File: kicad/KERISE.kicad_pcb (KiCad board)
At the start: 2 copper layers, 41 x 38.7 mm, 97 parts, among them J1 Motor_L, J10 ENC_Host, J11 ENC_Slave, J12 Host, J13 Slave, J14 Host, J15 Slave, J2 Motor_R, J3 Host, J4 Slave, J5 Host, J6 Slave, J7 COM, J8 ENC_Host, J9 ENC_Slave, P1 ToF_Host, P2 ToF_Slave, Q1 MTM231232LBF, Q10 MTM231232LBF, Q11 DMN3065LW-7, Q12 SFH3015FA, Q13 DMN3065LW-7, Q2 DMN3065LW-7, Q3 SFH3015FA, Q4 MTM231232LBF, Q5 DMN3065LW-7, Q6 SFH3015FA, Q7 MTM231232LBF, Q8 DMN3065LW-7, Q9 SFH3015FA, SW1 RESET, SW2 UPLOAD, U1 ESP32-PICO-D4, U2 DRV8835, U3 LXDC2UR30, U4 MA730, U5 MA730, U6 ICM-20602, U7 PCA9632, U8 VL6180X

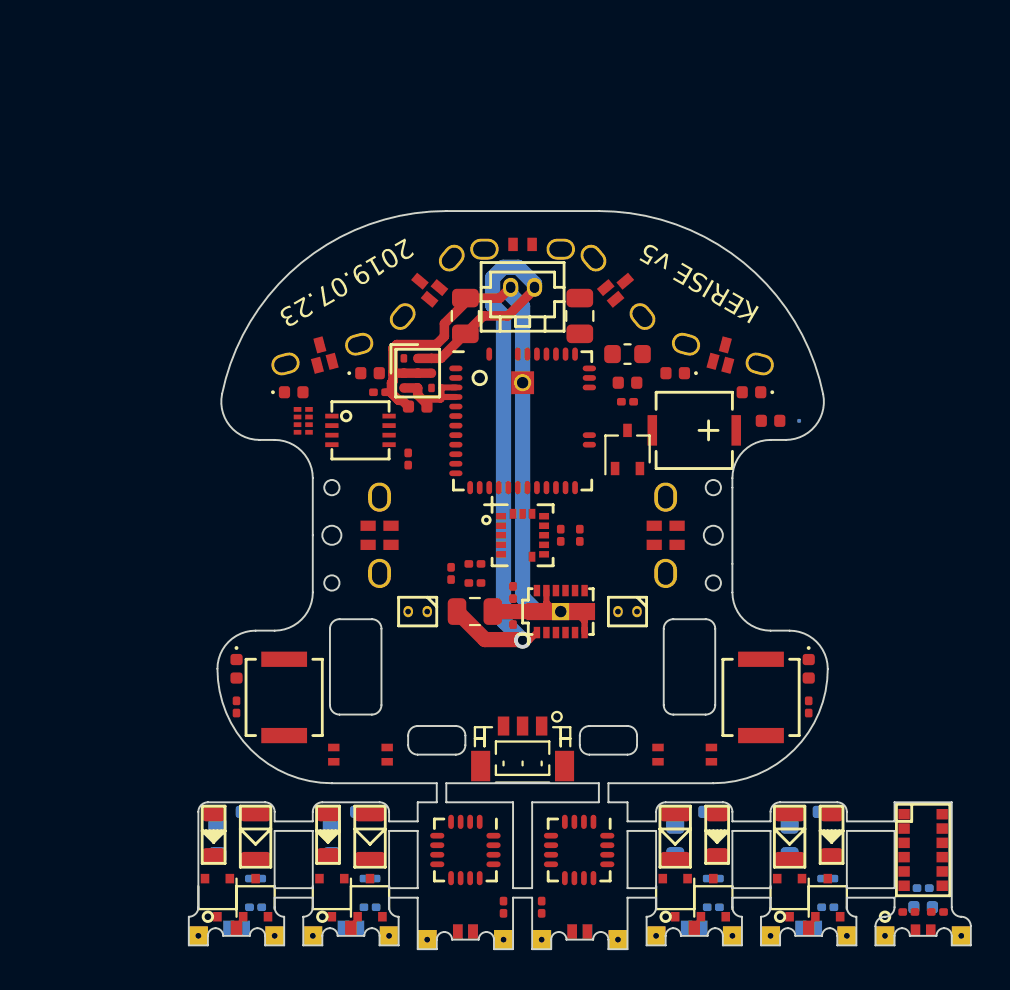
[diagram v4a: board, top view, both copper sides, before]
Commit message: fix pcb margin
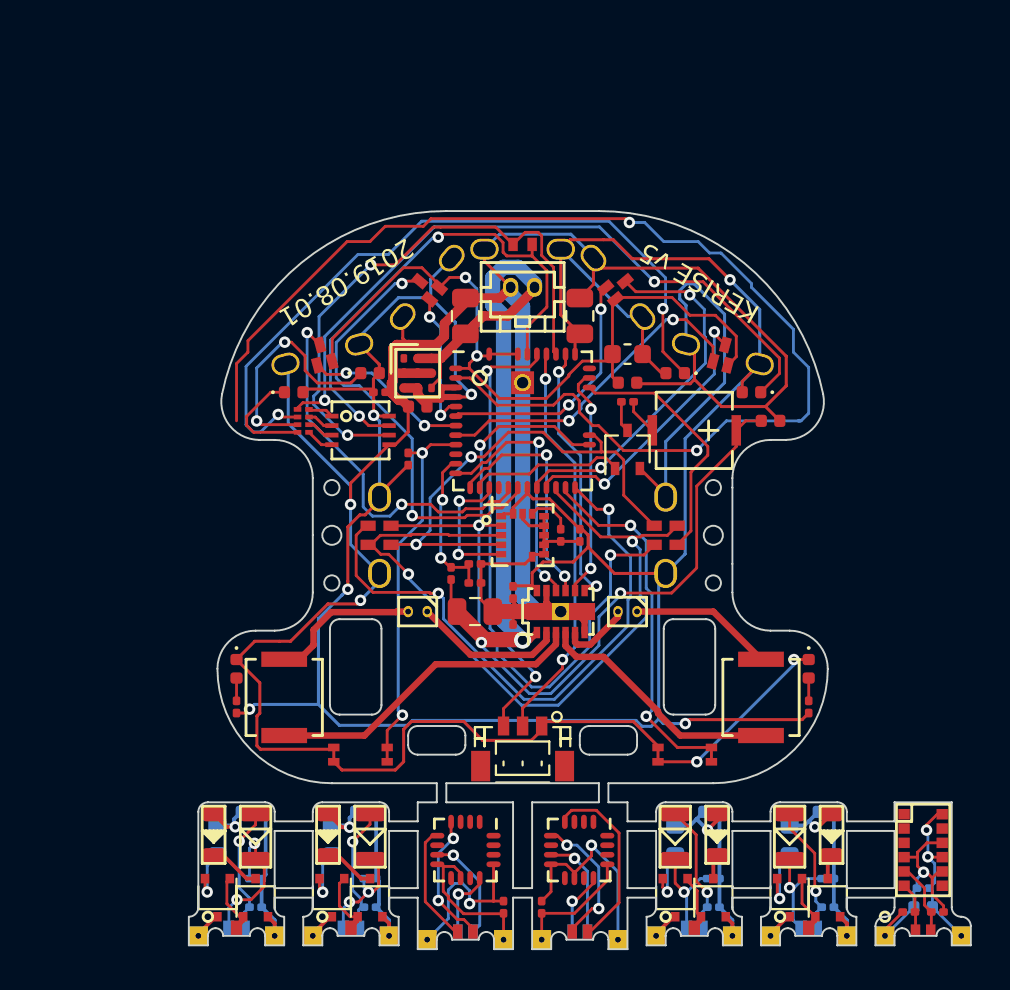
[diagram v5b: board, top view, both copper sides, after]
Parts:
- added G***: LOGO, mouse:KERI_9mm, B.Cu at (148.5, 111.0)
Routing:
- net +3V3: track 7.03 -> 151.0 mm, vias 0 -> 6
- net GND: track 40.0 -> 182.0 mm, vias 0 -> 4
- net /ANTENA: track 0.00 -> 64.7 mm, vias 0 -> 2
- net VDDA: track 0.00 -> 41.0 mm, vias 0 -> 2
- net SPI-MOSI: track 0.00 -> 39.9 mm, vias 0 -> 2
- net Net-(D8-Pad1): track 0.00 -> 38.3 mm, vias 0 -> 2
- net SPI-SCLK: track 0.00 -> 37.9 mm, vias 0 -> 3
- net Net-(D7-Pad1): track 0.00 -> 36.3 mm, vias 0 -> 2
- net SPI-CS-ENC_L: track 0.00 -> 31.0 mm, vias 0 -> 2
- net +BATT: track 35.3 -> 65.7 mm, vias 1 -> 3
- net I2C-SCL: track 0.00 -> 30.2 mm, vias 0 -> 2
- net I2C-SDA: track 0.00 -> 26.5 mm, vias 0 -> 2
- net SPI-MISO: track 0.00 -> 26.1 mm, vias 0 -> 2
- net UART-TX: track 0.00 -> 23.5 mm, vias 0 -> 2
- net PR-LED-SL: track 0.00 -> 23.3 mm, vias 0 -> 2
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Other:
- board text added: "2019.08.01"
- board text removed: "2019.07.23"

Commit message: 回路を修正，未配線
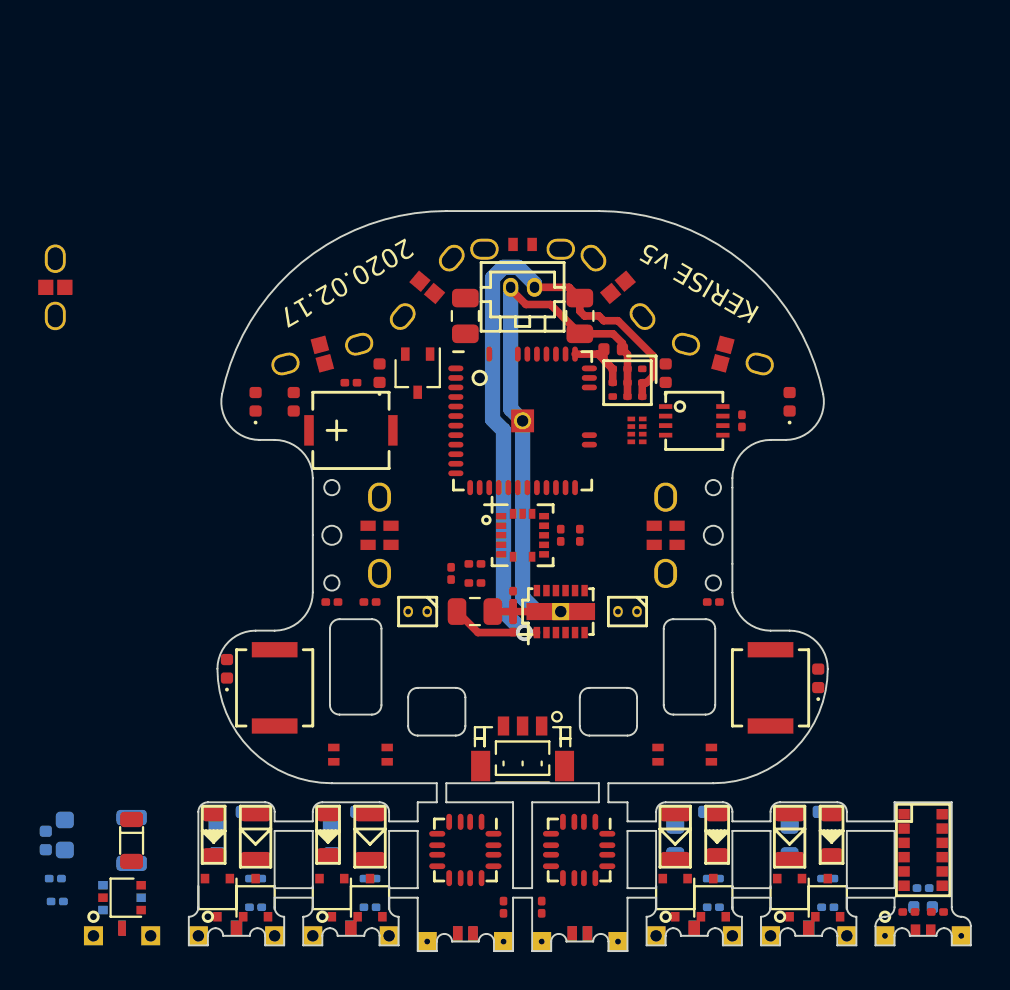
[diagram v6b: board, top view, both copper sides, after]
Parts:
- removed the C11 at (134.2, 127.5)
- removed the C12 at (134.5, 131.0)
- removed the C3 at (148.0, 118.0)
- removed the C8 at (154.0, 105.0)
- removed G***: LOGO, mouse:KERI_9mm
- removed the J3 at (143.5, 100.0)
- removed the J6 at (133.5, 134.0)
- removed L3: 100u, Inductor_SMD:L_0603_1608Metric
- added C10: 2.2u, Capacitor_SMD:C_0402_1005Metric, B.Cu at (123.5, 129.0)
- added C10: 2.2u, Capacitor_SMD:C_0402_1005Metric, B.Cu at (134.2, 127.5)
- added C11: 0.1u, Capacitor_SMD:C_0201_0603Metric, B.Cu at (124.0, 131.0)
- added C11: 0.1u, Capacitor_SMD:C_0201_0603Metric, B.Cu at (134.5, 131.0)
- added C5: 0.1u, Capacitor_SMD:C_0201_0603Metric, F.Cu at (146.0, 114.5)
- added D4: SFH4045N_L, mouse:SFH4045N_L, F.Cu at (128.0, 129.0)
- added J3: Host, mouse:IR_HOST_V_04, F.Cu at (124.0, 100.0)
- added J3: Host, mouse:IR_HOST_04, F.Cu at (143.5, 100.0)
- added J6: Slave, mouse:IR_SLAVE_04, F.Cu at (127.5, 134.0)
- added J6: Slave, mouse:IR_SLAVE_04, F.Cu at (133.5, 134.0)
- added Q4: MTM231232LBF, mouse:SOT-323_SC-70, B.Cu at (127.5, 132.0)
- added Q5: DMN3065LW-7, mouse:SOT-323_SC-70, F.Cu at (127.5, 132.0)
- added Q6: SFH3015FA_L, mouse:SFH3015FA_L, B.Cu at (128.0, 129.0)
- added R8: 100, Resistor_SMD:R_0603_1608Metric, B.Cu at (124.5, 128.7)
- added R9: 10k, Resistor_SMD:R_0201_0603Metric, B.Cu at (124.1, 132.2)
- AE1: moved to F.Cu
- C14: renamed from C15; value 1u -> 2.2u
- C16: renamed from C17; value 1u -> 2.2u
- C8: renamed from C9; value 1u -> 2.2u
- J12, J14, J5: footprint mouse:STAND_HOST_05 -> mouse:IR_HOST_04
- J13, J15, J4: footprint mouse:STAND_SLAVE_05 -> mouse:IR_SLAVE_04
- moved C21 25.0 mm to (136.5, 106.0), turned to 90 degrees
- moved C20 19.1 mm to (160.0, 107.0), turned to 270 degrees
- moved AE1 18.1 mm to (145.0, 104.8)
- moved LS1 18.0 mm to (139.5, 107.5), turned to 0 degrees
- moved RN1 17.5 mm to (154.5, 107.5)
- moved U7 17.5 mm to (157.5, 107.0)
- moved R14 14.5 mm to (139.5, 105.0), turned to 0 degrees
- moved Q13 11.7 mm to (143.0, 104.5), turned to 270 degrees
- moved U3 11.0 mm to (154.0, 105.0), turned to 0 degrees
- moved C1 10.7 mm to (153.2, 103.2), turned to 180 degrees
- moved R1 7.76 mm to (140.5, 116.5), turned to 180 degrees
- moved R4 7.43 mm to (138.5, 116.5), turned to 180 degrees
- moved R5 7.43 mm to (158.5, 116.5), turned to 0 degrees
- moved C6 6.00 mm to (151.5, 101.5), turned to 270 degrees
- moved C7 6.00 mm to (145.5, 101.5)
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- renumbered C13 to C12, C14 to C13, C16 to C15, C18 to C17, C19 to C18, C20 to C19, C21 to C20, C22 to C21, C23 to C22, C24 to C23, C4 to C3, C5 to C4, C10 to C9
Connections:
- C15 pad 1: /IR_RCV_FL/s_AVDD -> /IR_RCV_FL/s_3.3V
- C17 pad 1: /IR_RCV_FR/s_AVDD -> /IR_RCV_FR/s_3.3V
- C3 pad 1: +3V3 -> +BATT
- C4 pad 1: BAT-VOL -> +3V3
- C9 pad 1: /IR_RCV_SL/s_AVDD -> /IR_RCV_SL/s_3.3V
- J12 pad 2: VDDA -> PR-LED-FL
- J12 pad 3: PR-LED-FL -> PR-RCV-FL
- J12 pad 4: PR-RCV-FL -> GND
- J13 pad 2: /IR_RCV_FL/s_AVDD -> /IR_RCV_FL/s_IR_LED
- J13 pad 3: /IR_RCV_FL/s_IR_LED -> /IR_RCV_FL/s_IR_RCV
- J13 pad 4: /IR_RCV_FL/s_IR_RCV -> /IR_RCV_FL/s_GND
- J14 pad 2: VDDA -> PR-LED-FR
- J14 pad 3: PR-LED-FR -> PR-RCV-FR
- J14 pad 4: PR-RCV-FR -> GND
- J15 pad 2: /IR_RCV_FR/s_AVDD -> /IR_RCV_FR/s_IR_LED
- J15 pad 3: /IR_RCV_FR/s_IR_LED -> /IR_RCV_FR/s_IR_RCV
- J15 pad 4: /IR_RCV_FR/s_IR_RCV -> /IR_RCV_FR/s_GND
- J4 pad 2: /IR_RCV_SL/s_AVDD -> /IR_RCV_SL/s_IR_LED
- J4 pad 3: /IR_RCV_SL/s_IR_LED -> /IR_RCV_SL/s_IR_RCV
- J4 pad 4: /IR_RCV_SL/s_IR_RCV -> /IR_RCV_SL/s_GND
- J5 pad 2: VDDA -> PR-LED-SR
- J5 pad 3: PR-LED-SR -> PR-RCV-SR
- J5 pad 4: PR-RCV-SR -> GND
- Q1 pad 2: Net-(Q1-Pad2) -> /IR_RCV_SL/s_3.3V
- Q1 pad 3: /IR_RCV_SL/s_3.3V -> Net-(Q1-Pad3)
- Q10 pad 2: Net-(Q10-Pad2) -> /IR_RCV_FR/s_3.3V
- Q10 pad 3: /IR_RCV_FR/s_3.3V -> Net-(Q10-Pad3)
- Q12 pad 1: /IR_RCV_FR/s_AVDD -> /IR_RCV_FR/s_3.3V
- Q3 pad 1: /IR_RCV_SL/s_AVDD -> /IR_RCV_SL/s_3.3V
- Q4 pad 2: Net-(Q4-Pad2) -> /IR_RCV_SR/s_3.3V
- Q4 pad 3: /IR_RCV_SR/s_3.3V -> Net-(Q4-Pad3)
- Q6 pad 1: /IR_RCV_SR/s_AVDD -> /IR_RCV_SR/s_3.3V
- Q7 pad 2: Net-(Q7-Pad2) -> /IR_RCV_FL/s_3.3V
- Q7 pad 3: /IR_RCV_FL/s_3.3V -> Net-(Q7-Pad3)
- Q9 pad 1: /IR_RCV_FL/s_AVDD -> /IR_RCV_FL/s_3.3V
- R10 pad 1: Net-(Q7-Pad2) -> Net-(Q7-Pad3)
- R12 pad 1: Net-(Q10-Pad2) -> Net-(Q10-Pad3)
- R6 pad 1: Net-(Q1-Pad2) -> Net-(Q1-Pad3)
- R8 pad 1: Net-(Q4-Pad2) -> Net-(Q4-Pad3)
- U1 pad 1: VDDA -> +3V3
- U1 pad 43: VDDA -> +3V3
- U1 pad 46: VDDA -> +3V3
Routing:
- net GND: track 182.0 -> 33.3 mm, vias 4 -> 0
- net +3V3: track 151.0 -> 4.24 mm, vias 6 -> 0
- net /ANTENA: track 64.7 -> 0.00 mm, vias 2 -> 0
- net VDDA: track 41.0 -> 0.00 mm, vias 2 -> 0
- net SPI-MOSI: track 39.9 -> 0.00 mm, vias 2 -> 0
- net Net-(D8-Pad1): track 38.3 -> 0.00 mm, vias 2 -> 0
- net SPI-SCLK: track 37.9 -> 0.00 mm, vias 3 -> 0
- net Net-(D7-Pad1): track 36.3 -> 0.00 mm, vias 2 -> 0
- net SPI-CS-ENC_L: track 31.0 -> 0.00 mm, vias 2 -> 0
- net I2C-SCL: track 30.2 -> 0.00 mm, vias 2 -> 0
- net +BATT: track 65.7 -> 37.5 mm, vias 3 -> 1
- net I2C-SDA: track 26.5 -> 0.00 mm, vias 2 -> 0
- net SPI-MISO: track 26.1 -> 0.00 mm, vias 2 -> 0
- net UART-TX: track 23.5 -> 0.00 mm, vias 2 -> 0
- net PR-LED-SL: track 23.3 -> 0.00 mm, vias 2 -> 0
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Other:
- board size 41 x 38.7 mm -> 41 x 38.8 mm
- board text added: "2020.02.17"
- board text removed: "2019.08.01"

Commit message: 予備配線完了
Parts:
- removed AE1: Antenna, mouse:HIDDEN_PAD
- removed the C10 at (123.5, 129.0)
- removed the C10 at (134.2, 127.5)
- removed the C11 at (124.0, 131.0)
- removed the C11 at (134.5, 131.0)
- removed the D10 at (134.5, 106.0)
- removed the D4 at (128.0, 129.0)
- removed the D4 at (132.3, 128.7)
- removed the D9 at (141.0, 104.5)
- removed the J14 at (159.0, 103.5)
- removed the J15 at (157.5, 134.0)
- removed the J3 at (124.0, 100.0)
- removed the J3 at (143.5, 100.0)
- removed the J5 at (153.5, 100.0)
- removed the J6 at (127.5, 134.0)
- removed the J6 at (133.5, 134.0)
- removed Q10: MTM231232LBF, mouse:SOT-323_SC-70
- removed Q11: DMN3065LW-7, mouse:SOT-323_SC-70
- removed Q12: SFH3015FA, mouse:SFH3015FA
- removed Q13: DMN3065LW-7, Package_TO_SOT_SMD:SOT-323_SC-70
- removed the Q4 at (127.5, 132.0)
- removed the Q4 at (132.5, 132.0)
- removed the Q5 at (127.5, 132.0)
- removed the Q5 at (134.5, 132.0)
- removed the Q6 at (128.0, 129.0)
- removed the Q6 at (134.5, 128.8)
- removed the R13 at (158.5, 132.5)
- removed the R14 at (139.5, 105.0)
- removed the R8 at (124.5, 128.7)
- removed the R8 at (132.5, 129.0)
- removed the R9 at (124.1, 132.2)
- removed the R9 at (134.5, 132.5)
- removed the U6 at (148.5, 113.0)
- added C10: 2.2u, Capacitor_SMD:C_0402_1005Metric, F.Cu at (164.5, 132.0)
- added C11: 0.1u, Capacitor_SMD:C_0201_0603Metric, B.Cu at (165.0, 128.5)
- added D4: LED, LED_SMD:LED_0402_1005Metric, F.Cu at (139.5, 99.6)
- added D7: SFH4045N, mouse:SFH4045N_L, B.Cu at (133.8, 129.2)
- added D8: SFH4045N, mouse:SFH4045N_L, B.Cu at (139.8, 129.2)
- added J1: Host, mouse:IR_HOST_V_04, F.Cu at (159.5, 102.0)
- added J10: Host, mouse:IR_HOST_V_04, F.Cu at (154.5, 99.0)
- added J11: Slave, mouse:IR_SLAVE_V_04, F.Cu at (133.5, 134.0)
- added J2: Slave, mouse:IR_SLAVE_V_04, F.Cu at (157.5, 134.0)
- added J3: Host, mouse:IR_HOST_V_04, F.Cu at (137.5, 102.0)
- added Q4: DMN3065LW-7, mouse:SOT-323_SC-70, B.Cu at (163.5, 132.0)
- added Q5: SFH3015FA, mouse:SFH3015FA_L, B.Cu at (163.5, 129.2)
- added Q6: DMN3065LW-7, mouse:SOT-323_SC-70, F.Cu at (133.5, 132.0)
- added R11: 100, Resistor_SMD:R_0603_1608Metric, B.Cu at (138.1, 132.0)
- added R15: 1k, Resistor_SMD:R_0201_0603Metric, F.Cu at (141.0, 116.5)
- added R5: 100, Resistor_SMD:R_0603_1608Metric, F.Cu at (156.7, 132.0)
- added R9: 100, Resistor_SMD:R_0603_1608Metric, B.Cu at (132.2, 132.0)
- added U4: ICM-20602, mouse:ICM-20602, F.Cu at (148.5, 113.0)
- C15, C17, C8: moved to F.Cu
- D3: value SFH4045N -> LED; footprint mouse:SFH4045N -> LED_SMD:LED_0402_1005Metric
- D5, D6: footprint mouse:SFH4045N -> mouse:SFH4045N_L
- J12: footprint mouse:IR_HOST_04 -> mouse:IR_HOST_V_04
- J13, J4: footprint mouse:IR_SLAVE_04 -> mouse:IR_SLAVE_V_04
- Q1: value MTM231232LBF -> DMN3065LW-7; footprint mouse:SOT-323_SC-70 -> Package_TO_SOT_SMD:SOT-323_SC-70
- Q2: moved to B.Cu
- Q3: footprint mouse:SFH3015FA -> mouse:SFH3015FA_L; moved to B.Cu
- Q7: value MTM231232LBF -> SFH3015FA; footprint mouse:SOT-323_SC-70 -> mouse:SFH3015FA_L
- Q9: footprint mouse:SFH3015FA -> mouse:SFH3015FA_L
- R10, R12, R6: value 100 -> 10k; footprint Resistor_SMD:R_0603_1608Metric -> Resistor_SMD:R_0201_0603Metric
- R4: value 1k -> 10
- R7: value 10k -> 100; footprint Resistor_SMD:R_0201_0603Metric -> Resistor_SMD:R_0603_1608Metric; moved to F.Cu
- moved D3 31.4 mm to (145.0, 98.0)
- moved C15 29.5 mm to (135.0, 130.2), turned to 270 degrees
- moved C14 29.5 mm to (135.0, 128.5), turned to 270 degrees
- moved Q7 29.1 mm to (133.5, 129.2), turned to 90 degrees
- moved R10 28.0 mm to (134.8, 132.5), turned to 0 degrees
- moved Q1 27.9 mm to (143.0, 104.5)
- moved Q8 25.0 mm to (139.5, 132.0), turned to 180 degrees
- moved J13 24.0 mm to (139.5, 134.0)
- moved J4 24.0 mm to (163.5, 134.0)
- moved Q9 23.0 mm to (139.5, 129.2)
- moved R7 22.2 mm to (162.7, 132.0), turned to 90 degrees
- moved R6 20.5 mm to (159.0, 130.0)
- moved C8 18.8 mm to (158.5, 132.0), turned to 270 degrees
- moved C9 18.7 mm to (159.0, 128.5), turned to 270 degrees
- moved C17 17.5 mm to (141.0, 130.2), turned to 270 degrees
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- renumbered C13 to C12, C12 to C13, C5 to C18, C6 to C19, C22 to C2, C7 to C20, C2 to C21, C3 to C22, C4 to C23, C23 to C3, C20 to C4, C21 to C5, C18 to C6, C19 to C7, D7 to D1, D2 to D10, D8 to D2, D1 to D9, J1 to J14, J2 to J15, J10 to J5, J11 to J6, J8 to J7, J9 to J8, J7 to J9, R2 to R13, R3 to R14, R5 to R16, R15 to R2, R16 to R3, R11 to R8, U8 to U2, U7 to U3, U4 to U6, U3 to U7, U2 to U8
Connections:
- C14 pad 1: /IR_RCV_FL/LED_to_C -> /IR_RCV_SR/LED_to_C
- C14 pad 2: /IR_RCV_FL/s_GND -> /IR_RCV_SR/s_GND
- C15 pad 1: /IR_RCV_FL/s_3.3V -> /IR_RCV_SR/s_3.3V
- C15 pad 2: /IR_RCV_FL/s_GND -> /IR_RCV_SR/s_GND
- C16 pad 1: /IR_RCV_FR/LED_to_C -> /IR_RCV_SL/LED_to_C
- C16 pad 2: /IR_RCV_FR/s_GND -> /IR_RCV_SL/s_GND
- C17 pad 1: /IR_RCV_FR/s_3.3V -> /IR_RCV_SL/s_3.3V
- C17 pad 2: /IR_RCV_FR/s_GND -> /IR_RCV_SL/s_GND
- C8 pad 1: /IR_RCV_SL/LED_to_C -> /IR_RCV_FR/LED_to_C
- C8 pad 2: /IR_RCV_SL/s_GND -> /IR_RCV_FR/s_GND
- C9 pad 1: /IR_RCV_SL/s_3.3V -> /IR_RCV_FR/s_3.3V
- C9 pad 2: /IR_RCV_SL/s_GND -> /IR_RCV_FR/s_GND
- D3 pad 1: /IR_RCV_SL/LED_to_FET -> Net-(D3-Pad1)
- D3 pad 2: /IR_RCV_SL/LED_to_C -> +3V3
- D5 pad 1: /IR_RCV_FL/LED_to_FET -> /IR_RCV_FR/LED_to_FET
- D5 pad 2: /IR_RCV_FL/LED_to_C -> /IR_RCV_FR/LED_to_C
- D6 pad 1: /IR_RCV_FR/LED_to_FET -> /IR_RCV_FL/LED_to_FET
- D6 pad 2: /IR_RCV_FR/LED_to_C -> /IR_RCV_FL/LED_to_C
- D9 pad 2: Net-(D1-Pad2) -> Net-(D9-Pad2)
- J12 pad 2: PR-LED-FL -> PR-LED-SL
- J12 pad 3: PR-RCV-FL -> PR-RCV-SL
- J13 pad 1: /IR_RCV_FL/s_3.3V -> /IR_RCV_SL/s_3.3V
- J13 pad 2: /IR_RCV_FL/s_IR_LED -> /IR_RCV_SL/s_IR_LED
- J13 pad 3: /IR_RCV_FL/s_IR_RCV -> /IR_RCV_SL/s_IR_RCV
- J13 pad 4: /IR_RCV_FL/s_GND -> /IR_RCV_SL/s_GND
- J4 pad 1: /IR_RCV_SL/s_3.3V -> /IR_RCV_FL/s_3.3V
- J4 pad 2: /IR_RCV_SL/s_IR_LED -> /IR_RCV_FL/s_IR_LED
- J4 pad 3: /IR_RCV_SL/s_IR_RCV -> /IR_RCV_FL/s_IR_RCV
- J4 pad 4: /IR_RCV_SL/s_GND -> /IR_RCV_FL/s_GND
- Q1 pad 1: /IR_RCV_SL/s_IR_LED -> SPEAKER
- Q1 pad 2: /IR_RCV_SL/s_3.3V -> GND
- Q2 pad 1: /IR_RCV_SL/s_IR_LED -> /IR_RCV_FR/s_IR_LED
- Q2 pad 2: /IR_RCV_SL/s_GND -> /IR_RCV_FR/s_GND
- Q2 pad 3: /IR_RCV_SL/LED_to_FET -> /IR_RCV_FR/LED_to_FET
- Q3 pad 1: /IR_RCV_SL/s_3.3V -> /IR_RCV_FR/s_3.3V
- Q3 pad 2: /IR_RCV_SL/s_IR_RCV -> /IR_RCV_FR/s_IR_RCV
- Q7 pad 1: /IR_RCV_FL/s_IR_LED -> /IR_RCV_SR/s_3.3V
- Q7 pad 2: /IR_RCV_FL/s_3.3V -> /IR_RCV_SR/s_IR_RCV
- Q8 pad 1: /IR_RCV_FL/s_IR_LED -> /IR_RCV_SL/s_IR_LED
- Q8 pad 2: /IR_RCV_FL/s_GND -> /IR_RCV_SL/s_GND
- Q8 pad 3: /IR_RCV_FL/LED_to_FET -> /IR_RCV_SL/LED_to_FET
- Q9 pad 1: /IR_RCV_FL/s_3.3V -> /IR_RCV_SL/s_3.3V
- Q9 pad 2: /IR_RCV_FL/s_IR_RCV -> /IR_RCV_SL/s_IR_RCV
- R10 pad 1: Net-(Q7-Pad3) -> /IR_RCV_SR/s_IR_RCV
- R10 pad 2: /IR_RCV_FL/LED_to_C -> /IR_RCV_SR/s_GND
- R12 pad 1: Net-(Q10-Pad3) -> /IR_RCV_SL/s_IR_RCV
- R12 pad 2: /IR_RCV_FR/LED_to_C -> /IR_RCV_SL/s_GND
- R4 pad 1: +3V3 -> Net-(LS1-Pad2)
- R4 pad 2: Net-(D1-Pad2) -> Net-(Q1-Pad3)
- R6 pad 1: Net-(Q1-Pad3) -> /IR_RCV_FR/s_IR_RCV
- R6 pad 2: /IR_RCV_SL/LED_to_C -> /IR_RCV_FR/s_GND
- R7 pad 1: /IR_RCV_SL/s_IR_RCV -> /IR_RCV_FL/s_3.3V
- R7 pad 2: /IR_RCV_SL/s_GND -> /IR_RCV_FL/LED_to_C
- RN1 pad 7: Net-(D9-Pad1) -> Net-(D3-Pad1)
- U1 pad 2: /ANTENA -> (no net)
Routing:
- net /IR_RCV_FR/s_3.3V: track 0.00 -> 9.63 mm
- net /IR_RCV_FL/s_3.3V: track 0.00 -> 9.63 mm
- net /IR_RCV_SL/s_GND: track 0.00 -> 9.12 mm
- net /IR_RCV_SR/s_GND: track 0.00 -> 9.02 mm
- net /IR_RCV_FL/LED_to_FET: track 0.00 -> 7.77 mm, vias 0 -> 1
- net /IR_RCV_SR/s_3.3V: track 0.00 -> 7.74 mm
- net /IR_RCV_FR/LED_to_FET: track 0.00 -> 7.71 mm, vias 0 -> 1
- net /IR_RCV_SL/s_3.3V: track 0.00 -> 7.68 mm
- net /IR_RCV_FR/s_GND: track 0.00 -> 7.58 mm, vias 0 -> 2
- net /IR_RCV_FL/s_GND: track 0.00 -> 7.41 mm, vias 0 -> 2
- net /IR_RCV_SL/s_IR_RCV: track 0.00 -> 7.29 mm, vias 0 -> 1
- net /IR_RCV_SR/s_IR_RCV: track 0.00 -> 6.93 mm, vias 0 -> 1
- net /IR_RCV_FR/s_IR_RCV: track 0.00 -> 6.23 mm
- net /IR_RCV_FL/s_IR_RCV: track 0.00 -> 6.10 mm
- net /IR_RCV_SL/LED_to_C: track 0.00 -> 5.05 mm
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- added copper zone on F.Cu, net /IR_RCV_FL/LED_to_FET
- added copper zone on B.Cu, net /IR_RCV_FL/s_3.3V
- added copper zone on F.Cu, net /IR_RCV_FR/LED_to_FET
- added copper zone on B.Cu, net /IR_RCV_FR/s_3.3V
- added copper zone on B.Cu, net /IR_RCV_SL/LED_to_C
- added copper zone on F.Cu, net /IR_RCV_SL/s_3.3V
- added copper zone on B.Cu, net /IR_RCV_SR/LED_to_C
- added copper zone on F.Cu, net /IR_RCV_SR/s_3.3V
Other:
- board size 41 x 38.8 mm -> 40.5 x 38.8 mm
- board text added: "2020.02.20"
- board text removed: "2020.02.17"

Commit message: 自動配線完了
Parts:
- moved C10 0.25 mm to (164.5, 132.2)
- moved C8 0.25 mm to (158.5, 132.2)
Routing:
- net /Motor/MT_OUT_L_L: track 0.00 -> 18.3 mm
- net /Motor/MT_OUT_L_R: track 0.00 -> 14.4 mm
- net /Motor/MT_OUT_L1: track 0.00 -> 8.20 mm
- net /Motor/MT_OUT_L2: track 0.00 -> 7.83 mm
- net /Motor/MT_OUT_R1: track 0.00 -> 7.83 mm
- net /Motor/MT_OUT_R2: track 0.00 -> 3.91 mm
- net /IR_RCV_FL/LED_to_FET: track 7.77 -> 5.56 mm
- net /IR_RCV_FR/LED_to_FET: track 7.71 -> 5.56 mm
- net GND: track 33.3 -> 35.3 mm
- net /IR_RCV_FR/s_GND: track 7.58 -> 6.35 mm
- net /IR_RCV_FL/s_GND: track 7.41 -> 6.45 mm
- net /IR_RCV_FL/LED_to_C: track 2.88 -> 3.85 mm
- net /IR_RCV_SL/LED_to_FET: track 2.68 -> 3.56 mm
- net /IR_RCV_SR/LED_to_FET: track 2.76 -> 3.56 mm
- net /IR_RCV_FR/LED_to_C: track 2.88 -> 3.53 mm
- added copper zone on F.Cu, net /IR_RCV_FL/LED_to_C
- added copper zone on F.Cu, net /IR_RCV_FR/LED_to_C
- removed copper zone on F.Cu, net /IR_RCV_FL/LED_to_FET
- removed copper zone on F.Cu, net /IR_RCV_FR/LED_to_FET
